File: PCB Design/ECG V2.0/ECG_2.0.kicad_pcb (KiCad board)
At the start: 4 copper layers, 42.3 x 69.7 mm, 50 parts, among them J1 01x05_Female, J2 JST_01x04_Male, U1 Li-Po, U10 ESP32-C3-MINI-1-N4, U11 FS8205A, U12 DW01, U2 TP4056-C21417, U3 USBLC6-2SC6, U4 Battery_Switch, U5 5V_switch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

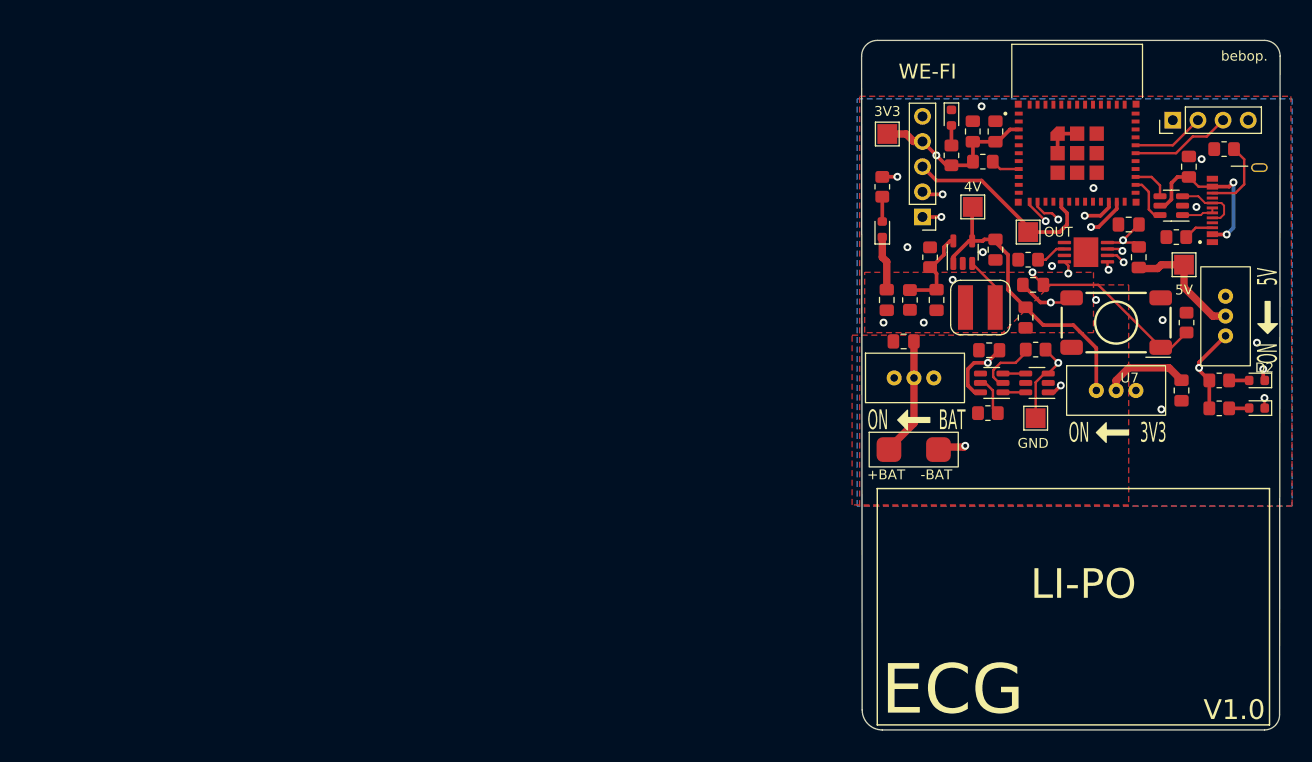
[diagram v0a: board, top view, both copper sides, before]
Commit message: added li-po and esp32 to models
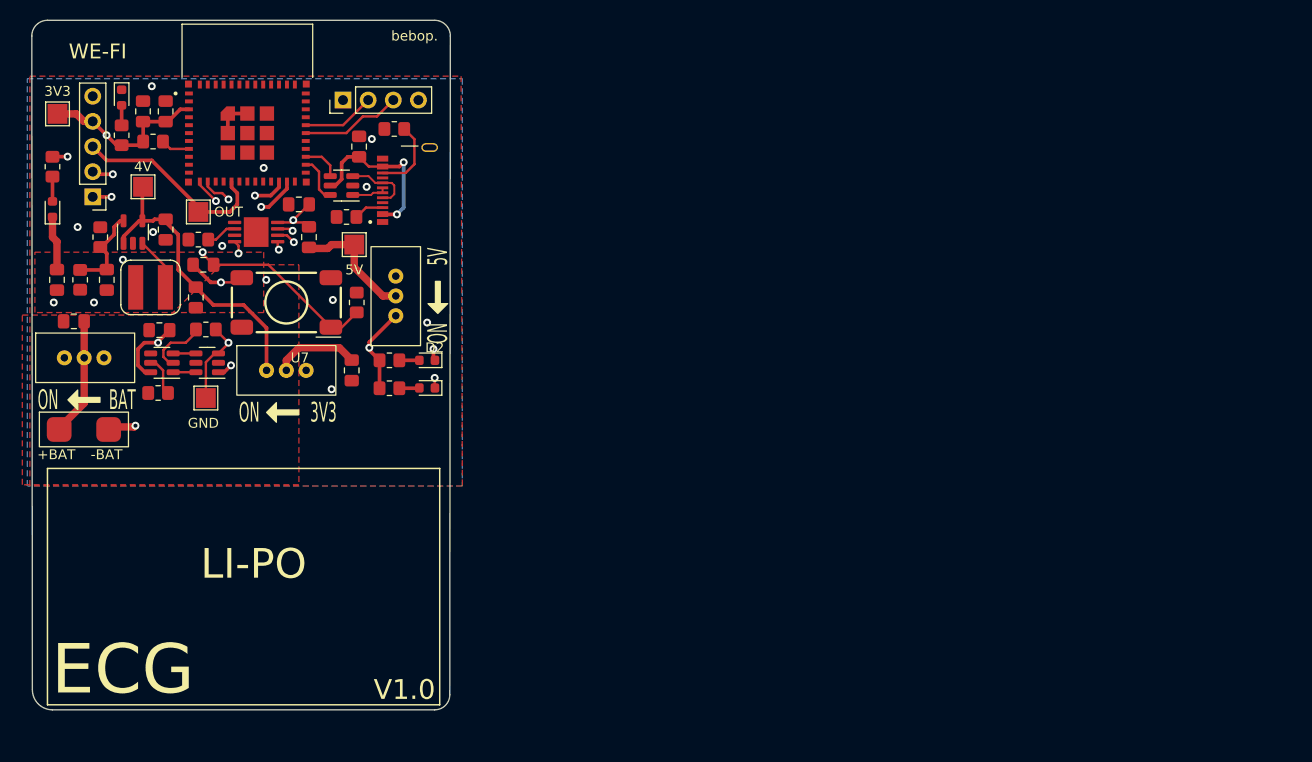
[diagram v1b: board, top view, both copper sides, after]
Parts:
- moved 4V 83.8 mm to (141.2, 83.8)
- moved C10 83.8 mm to (143.5, 76.2)
- moved C11 83.8 mm to (163.1, 79.8)
- moved C6 83.8 mm to (143.5, 88.1)
- moved C9 83.8 mm to (141.2, 76.2)
- moved D1 83.8 mm to (169.9, 101.3)
- moved D2 83.8 mm to (169.9, 104.1)
- moved J2 83.8 mm to (161.4, 75.1)
- moved L1 83.8 mm to (142.0, 94.0)
- moved R11 83.8 mm to (142.7, 104.6)
- moved U10 83.8 mm to (151.8, 75.7)
- moved 3V3 83.8 mm to (132.6, 76.5)
- moved 5V 83.8 mm to (162.6, 89.7)
- moved C1 83.8 mm to (147.3, 91.7)
- moved C12 83.8 mm to (158.0, 88.9)
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
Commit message: Improved PCB design and Improved renderings
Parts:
- moved 3V3 37.9 mm to (160.2, 102.5)
- moved U7 32.6 mm to (132.8, 79.1), turned to -90 degrees
- moved 4V 29.1 mm to (163.6, 102.5)
- moved D4 28.4 mm to (153.9, 99.1), turned to 180 degrees
- moved C1 26.8 mm to (166.9, 110.0), turned to -90 degrees
- moved D3 24.5 mm to (153.9, 97.0), turned to 180 degrees
- moved R4 23.6 mm to (150.1, 97.0), turned to 0 degrees
- moved R7 23.3 mm to (150.1, 99.1), turned to 0 degrees
- moved GND 19.7 mm to (167.1, 102.5)
- moved C3 19.7 mm to (146.6, 102.4), turned to -90 degrees
- moved C13 19.5 mm to (136.7, 78.2)
- moved C2 18.5 mm to (143.8, 102.4), turned to 90 degrees
- moved J1 16.2 mm to (152.1, 87.4), turned to -90 degrees
- moved U4 16.1 mm to (148.8, 109.7)
- moved R3 16.0 mm to (150.1, 103.1)
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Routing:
- net +3V3: track 23.1 -> 71.7 mm
- net BTN: track 27.8 -> 44.0 mm
- net +LO: track 22.4 -> 7.11 mm, vias 2 -> 0
- net -LO: track 21.9 -> 8.73 mm, vias 2 -> 0
- net GND: track 18.1 -> 6.61 mm, vias 11 -> 0
- net +4V: track 30.4 -> 41.3 mm, vias 0 -> 2
- net BatO: track 11.7 -> 21.9 mm
- net /TX: track 7.35 -> 16.8 mm, vias 0 -> 1
- net Output: track 20.5 -> 12.6 mm
- net Net-(D2-Pad1): track 23.9 -> 16.3 mm, vias 2 -> 0
- net LED: track 22.8 -> 15.7 mm
- net /RX: track 10.2 -> 17.2 mm, vias 0 -> 1
- net Net-(D1-Pad1): track 23.2 -> 16.8 mm, vias 2 -> 0
- net In_5V: track 39.2 -> 44.9 mm, vias 2 -> 0
- net Net-(L1-Pad1): track 5.41 -> 0.00 mm
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- added copper zone on F.Cu, net +4V
- added copper zone on In1.Cu, net +BATT
- added copper zone on F.Cu, net Net-(L1-Pad1)
- added copper zone on F.Cu, net VSS
- removed copper zone on In1.Cu, net +3V3
- removed copper zone on In1.Cu, net VSS
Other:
- board text added: "3V3"
- board text added: "Battery protection"
- board text added: "Buck"
- board text added: "PROG"
- board text added: "SCAN"
- board text added: "STDBY"
- board text removed: "WE-FI"
- board text removed: "bebop."

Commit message: connections issue on pcb deisgn
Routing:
- net +4V: track 41.3 -> 44.4 mm
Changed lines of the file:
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@@
   (segment (start 147.498 111.328) (end 148.844 109.982) (width 1.25) (layer "F.Cu") (net 6))
   (segment (start 132.774 108.458) (end 135.644 111.328) (width 1.25) (layer "F.Cu") (net 6))
+  (segment (start 135.579249 93.104) (end 133.6885 91.213251) (width 0.25) (layer "F.Cu") (net 7))
   (segment (start 163.576 101.092) (end 163.576 102.5144) (width 0.25) (layer "F.Cu") (net 7))
   (segment (start 136.5465 77.089) (end 136.652 77.1945) (width 0.25) (layer "F.Cu") (net 7))
   (segment (start 162.052 99.568) (end 163.576 101.092) (width 0.25) (layer "F.Cu") (net 7))
+  (segment (start 133.6885 91.213251) (end 133.6885 91.204) (width 0.25) (layer "F.Cu") (net 7))
   (segment (start 132.842 77.089) (end 136.5465 77.089) (width 0.25) (layer "F.Cu") (net 7))
+  (segment (start 135.9635 93.104) (end 135.579249 93.104) (width 0.25) (layer "F.Cu") (net 7))
   (via (at 132.461 89.281) (size 0.8) (drill 0.4) (layers "F.Cu" "B.Cu") (free) (net 7))
   (via (at 162.052 99.568) (size 0.8) (drill 0.4) (layers "F.Cu" "B.Cu") (free) (net 7))

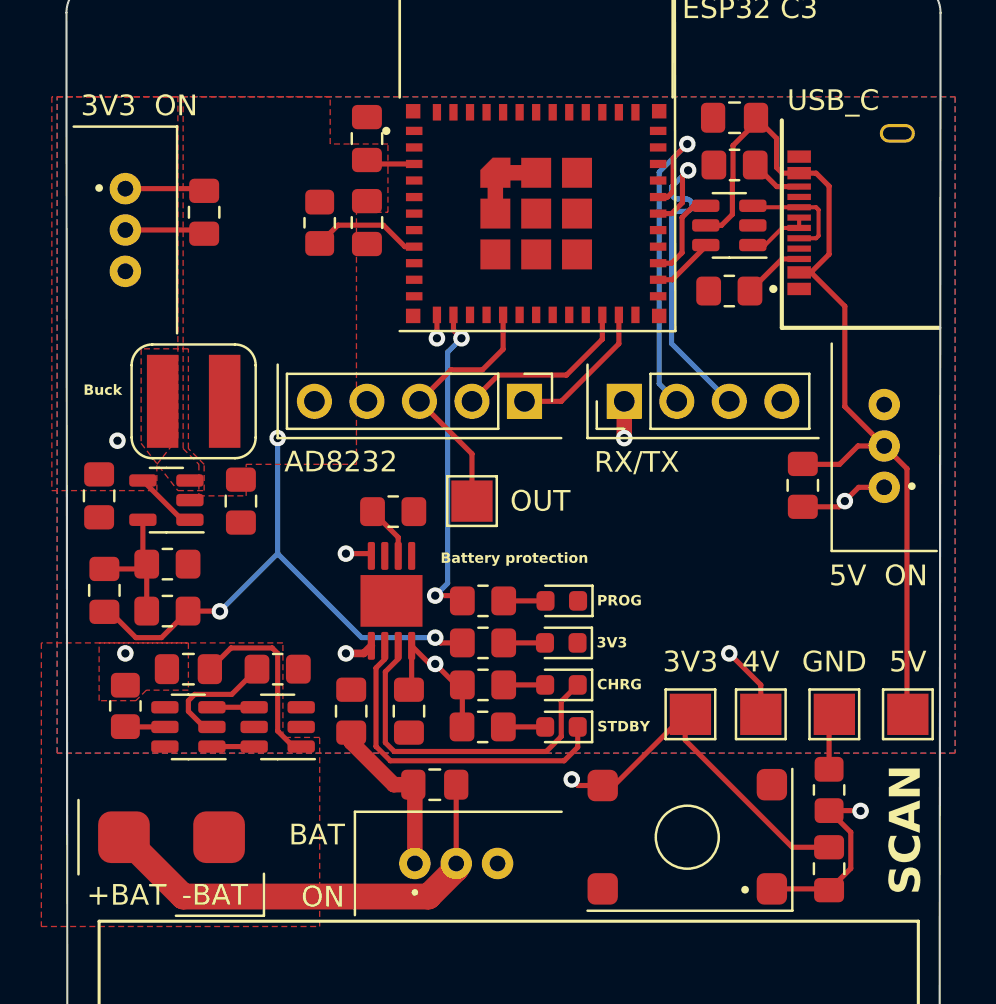
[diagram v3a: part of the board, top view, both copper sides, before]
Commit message: updated Schematic to reflect hardware testing issues
Changed schematic for USB-C, had the pin our wrong.

Changed through hole switch components and USB-C through hole for better fit.
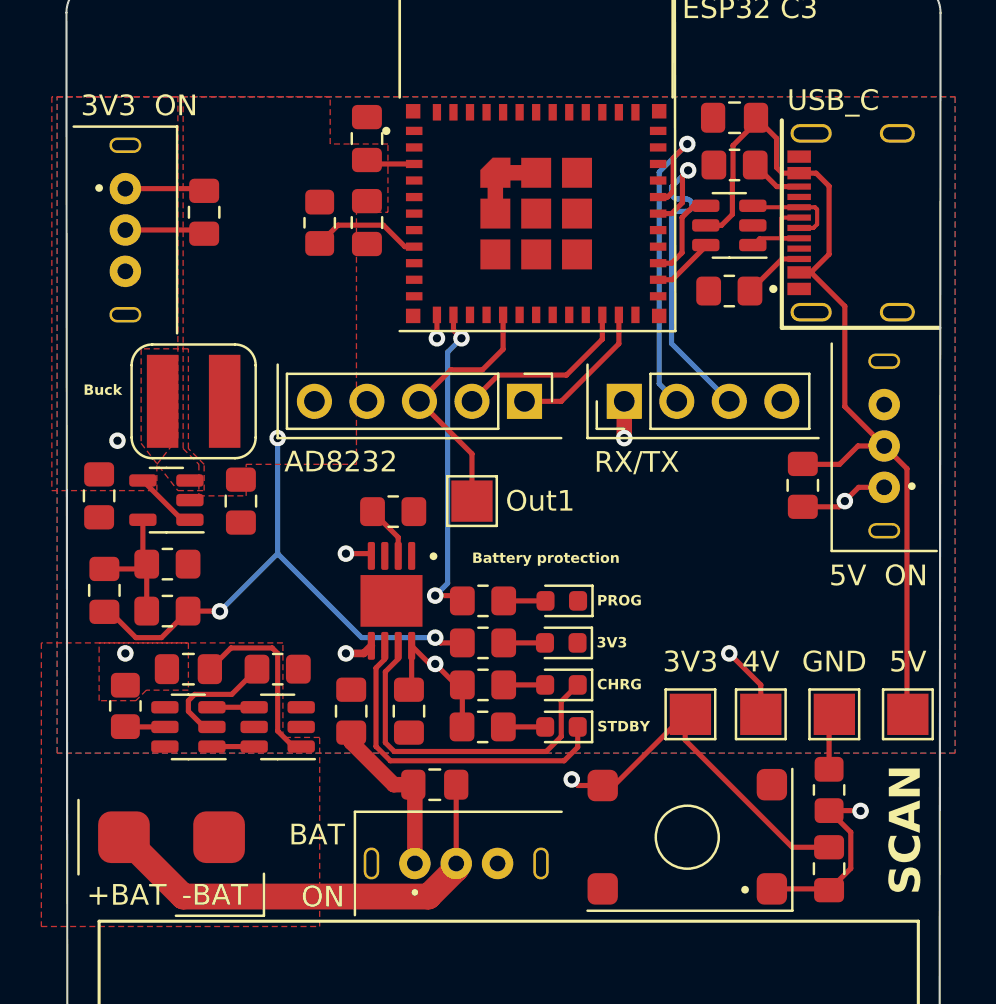
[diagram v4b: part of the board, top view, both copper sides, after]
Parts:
- renumbered OUT to Out1
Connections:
- U9 pad A6: DN -> DP
- U9 pad B7: DP -> DN
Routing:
- net DN: track 3.08 -> 5.07 mm
- net DP: track 5.51 -> 4.85 mm
